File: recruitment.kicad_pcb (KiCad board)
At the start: 2 copper layers, 1 part

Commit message: inizio progettazione circuito
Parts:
- removed C1: 1F, Capacitor_SMD:C_0805_2012Metric
- added J1: Screw_Terminal_01x01, TerminalBlock:TerminalBlock_Altech_AK300-2_P5.00mm, F.Cu at (156.5, 86.5)
- added K1: Relay_SPST-NO, Relay_THT:Relay_1-Form-A_Schrack-RYII_RM5mm, F.Cu at (120.6, 91.1)
- added U1: ACS781xLRTR-100U, Sensor_Current:Allegro_PSOF-7_4.8x6.4mm_P1.60mm, F.Cu at (145.6, 74.5)
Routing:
- net Net-(C1-Pad1): track 57.5 -> 0.00 mm

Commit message: giorno 2 : prime prove e footprint
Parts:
- added R1: R_US, Resistor_THT:R_Axial_DIN0204_L3.6mm_D1.6mm_P2.54mm_Vertical, F.Cu at (178.5, 110.5)
- added R2: R_Trim, Potentiometer_THT:Potentiometer_Piher_PT-6-H_Horizontal, F.Cu at (178.5, 94.2)
- added U2: LM317_TO-220, Package_TO_SOT_THT:TO-220-3_Vertical, F.Cu at (167.9, 110.5)
- added U3: TL084, Package_DIP:CERDIP-16_W7.62mm_SideBrazed, F.Cu at (155.4, 94.7)
- U1: value ACS781xLRTR-100U -> ACS780xLRTR-050B
- moved U1 59.0 mm to (192.0, 111.0)
- moved J1 38.2 mm to (193.5, 96.0)
- moved K1 37.6 mm to (158.1, 90.3)
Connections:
- net VCC renamed VPower
- K1 pad A2: unconnected-(K1-PadA2) -> GND
- U1 pad 1: unconnected-(U1-VCC-Pad1) -> +5V
- U1 pad 2: unconnected-(U1-GND-Pad2) -> GND
- U1 pad 3: unconnected-(U1-VOUT-Pad3) -> VHall
- U1 pad 4: unconnected-(U1-NC-Pad4) -> GND
- U1 pad 7: unconnected-(U1-NC-Pad7) -> GND

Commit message: prima prova pcb
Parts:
- added J2: ~, TerminalBlock:TerminalBlock_Altech_AK300-2_P5.00mm, F.Cu at (143.3, 90.5)
- added Q1: IRF9540N, Package_TO_SOT_THT:TO-220-3_Vertical, F.Cu at (143.0, 60.5)
- added Q2: BC337, Package_TO_SOT_THT:TO-92_Inline, F.Cu at (154.0, 59.0)
- added Q3: BC327, Package_TO_SOT_THT:TO-92_Inline, F.Cu at (156.5, 63.6)
- added R10: R_US, Resistor_SMD:R_1206_3216Metric, F.Cu at (185.1, 78.9)
- added R11: 10k, Resistor_SMD:R_1206_3216Metric, F.Cu at (149.0, 57.5)
- added R12: 10k, Resistor_SMD:R_1206_3216Metric, F.Cu at (162.0, 57.5)
- added R13: 10k, Resistor_SMD:R_1206_3216Metric, F.Cu at (149.0, 61.5)
- added R14: 10k, Resistor_SMD:R_1206_3216Metric, F.Cu at (149.1, 65.5)
- added R3: R_US, Resistor_SMD:R_1206_3216Metric, F.Cu at (174.5, 79.0)
- added R4: R_US, Resistor_SMD:R_1206_3216Metric, F.Cu at (174.5, 82.0)
- added R5: R_US, Resistor_SMD:R_1206_3216Metric, F.Cu at (174.5, 75.0)
- added R6: R_US, Resistor_SMD:R_1206_3216Metric, F.Cu at (178.5, 70.0)
- added R7: R_US, Resistor_SMD:R_1206_3216Metric, F.Cu at (185.1, 69.0)
- added R8: R_US, Resistor_SMD:R_1206_3216Metric, F.Cu at (185.1, 72.3)
- added R9: R_US, Resistor_SMD:R_1206_3216Metric, F.Cu at (185.1, 75.6)
- added RT1: 10k, Potentiometer_THT:Potentiometer_ACP_CA6-H2,5_Horizontal, F.Cu at (160.5, 60.5)
- added S1: ACS780xLRTR-050B, Sensor_Current:Allegro_PSOF-7_4.8x6.4mm_P1.60mm, F.Cu at (151.0, 89.0)
- added U4: 74LVC1G373, Package_TO_SOT_SMD:SOT-23-6, F.Cu at (168.5, 58.1)
- J1: value Screw_Terminal_01x01 -> ~
- K1: value Relay_SPST-NO -> Panasonic_ALFG2PF091; footprint Relay_THT:Relay_1-Form-A_Schrack-RYII_RM5mm -> Relay_THT:Relay_SPST_Panasonic_ALFG_FormA_CircularHoles
- R1: footprint Resistor_THT:R_Axial_DIN0204_L3.6mm_D1.6mm_P2.54mm_Vertical -> Resistor_SMD:R_1206_3216Metric
- R2: value R_Trim -> R_US; footprint Potentiometer_THT:Potentiometer_Piher_PT-6-H_Horizontal -> Resistor_SMD:R_1206_3216Metric
- U1: value ACS780xLRTR-050B -> LM7805_TO220; footprint Sensor_Current:Allegro_PSOF-7_4.8x6.4mm_P1.60mm -> Package_TO_SOT_THT:TO-220-3_Vertical
- U2: value LM317_TO-220 -> OP275; footprint Package_TO_SOT_THT:TO-220-3_Vertical -> Package_SO:SOIC-8_3.9x4.9mm_P1.27mm
- U3: value TL084 -> OP275; footprint Package_DIP:CERDIP-16_W7.62mm_SideBrazed -> Package_SO:SOIC-8_3.9x4.9mm_P1.27mm
- moved U1 54.3 mm to (176.5, 58.9), turned to -90 degrees
- moved U2 37.6 mm to (170.0, 73.0), turned to 90 degrees
- moved U3 33.7 mm to (169.5, 64.0), turned to 180 degrees
- moved J1 30.4 mm to (163.5, 91.0), turned to 180 degrees
- moved R1 30.0 mm to (169.0, 82.0)
- moved K1 28.6 mm to (138.5, 69.6)
- moved R2 18.0 mm to (169.0, 79.0), turned to 180 degrees
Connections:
- J1 pad 1: Net-(J1-Pin_1) -> Power
- J1 pad 2: (no net) -> Net-(J1-Pin_2)
- K1 pad 11: (no net) -> Net-(S1-IP+)
- K1 pad 14: VPower -> Power
- K1 pad A1: unconnected-(K1-PadA1) -> relé_bobina
- R1 pad 1: +5V -> Power
- R1 pad 2: Net-(U2-ADJ) -> Net-(U3A--)
- R2 pad 1: Net-(U2-ADJ) -> Net-(U3A--)
- U1 pad 1: +5V -> VMonitor
- U1 pad 3: VHall -> +5V
- U2 pad 1: Net-(U2-ADJ) -> Net-(U2B--)
- U2 pad 2: +5V -> Net-(U2A--)
- U2 pad 3: VMonitor -> Net-(U2A-+)
- U3 pad 1: Net-(U3A--) -> Net-(U2B-+)
- U3 pad 3: VHall -> Net-(U3A-+)
- U3 pad 4: +5V -> GND
- U3 pad 5: unconnected-(U3B-+-Pad5) -> Net-(U3B-+)
- U3 pad 6: unconnected-(U3B---Pad6) -> Net-(Q3-C)
- U3 pad 7: unconnected-(U3-Pad7) -> Net-(R14-Pad2)
- U3 pad 8: unconnected-(U3-Pad8) -> +5V
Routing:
- net Net-(J1-Pin_2): track 0.00 -> 19.8 mm
- net Load: track 0.00 -> 14.2 mm
- net Net-(S1-IP+): track 0.00 -> 11.8 mm
- net Power: track 0.00 -> 9.74 mm
- net Net-(Q2-C): track 0.00 -> 0.78 mm

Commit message: V1.0.0 : prima versione (si spera) funzionante
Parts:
- moved R7 22.5 mm to (169.1, 84.8), turned to 180 degrees
- moved R10 15.9 mm to (169.2, 78.8), turned to 180 degrees
- moved R6 14.9 mm to (169.2, 81.6)
- moved R2 10.5 mm to (174.5, 88.0)
- moved R9 7.35 mm to (178.0, 77.5), turned to 90 degrees
- moved R5 7.20 mm to (176.2, 82.0), turned to 0 degrees
- moved R8 7.12 mm to (178.0, 72.0), turned to 90 degrees
- moved R3 7.06 mm to (175.0, 72.0), turned to 90 degrees
- moved R1 6.26 mm to (174.5, 85.0)
- moved R4 4.56 mm to (175.0, 77.5), turned to -90 degrees
- moved R14 4.00 mm to (149.0, 61.5)
- moved R13 3.50 mm to (149.0, 65.0)
- moved S1 1.00 mm to (151.0, 88.0)
- moved U3 0.78 mm to (170.1, 64.5), turned to 90 degrees
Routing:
- net +5V: track 0.00 -> 100.1 mm, vias 0 -> 2
- net VMonitor: track 0.00 -> 54.7 mm
- net GND: track 0.00 -> 40.0 mm
- net Net-(U3A--): track 0.00 -> 34.4 mm
- net relé_bobina: track 0.00 -> 33.6 mm
- net Net-(Q3-C): track 0.00 -> 24.3 mm
- net Net-(U2B-+): track 0.00 -> 24.2 mm
- net Net-(R14-Pad2): track 0.00 -> 20.5 mm
- net Net-(U4-D): track 0.00 -> 19.1 mm, vias 0 -> 2
- net Net-(Q2-C): track 0.78 -> 18.2 mm
- net Net-(U2A-+): track 0.00 -> 16.8 mm
- net VoSensore: track 0.00 -> 16.4 mm
- net Net-(U3A-+): track 0.00 -> 15.2 mm, vias 0 -> 2
- net Net-(U3B-+): track 0.00 -> 12.4 mm
- net Power: track 9.74 -> 22.0 mm
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- added copper zone on F.Cu, net GND
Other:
- board outline added: 51 x 46 mm

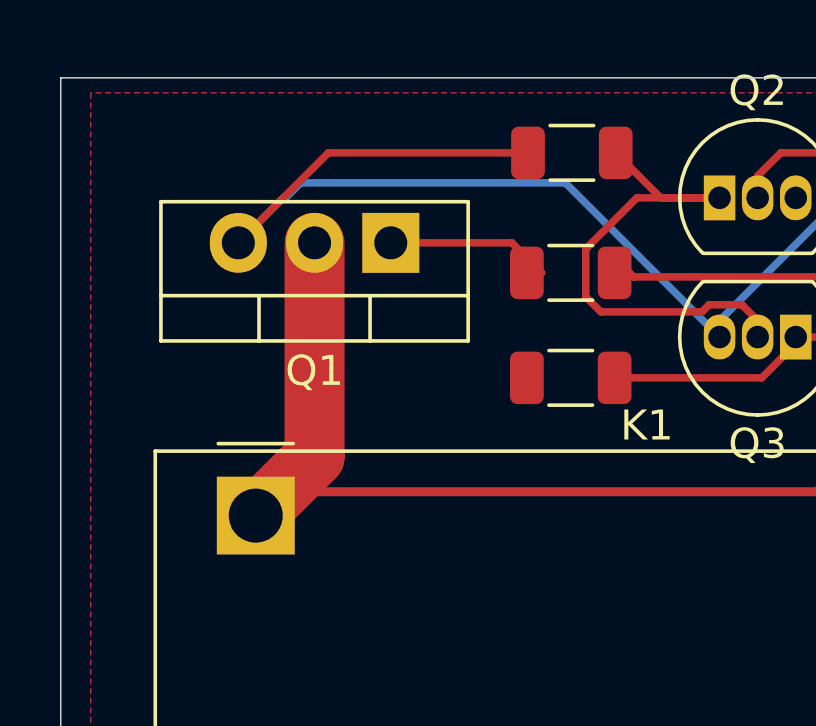
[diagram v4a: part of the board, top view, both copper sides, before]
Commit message: Aggiunto pin d'ingresso per Vmonitor, due diversi al posto di una per due perche mi dava problemi sulle distanze minime.
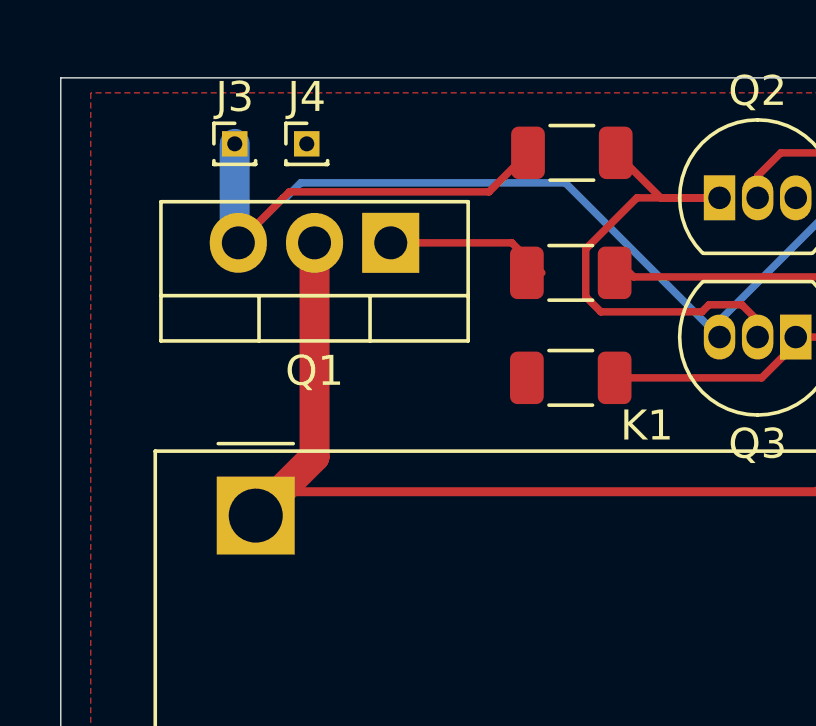
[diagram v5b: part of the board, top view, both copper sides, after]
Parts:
- added J3: Conn_01x01_Pin, Connector_PinHeader_1.00mm:PinHeader_1x01_P1.00mm_Vertical, F.Cu at (137.8, 57.2)
- added J4: Conn_01x01_Pin, Connector_PinHeader_1.00mm:PinHeader_1x01_P1.00mm_Vertical, F.Cu at (140.2, 57.2)
- R1: value R_US -> 120k
- R10: value R_US -> 51k
- R2: value R_US -> 11k
- R3: value R_US -> 6.8k
- R4, R5, R6: value R_US -> 10k
- R7: value R_US -> 51
- R8, R9: value R_US -> 20k
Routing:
- net VMonitor: track 54.7 -> 58.8 mm
